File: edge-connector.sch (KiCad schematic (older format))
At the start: 3 parts, among them J5 SFF-TA-1002-4C+

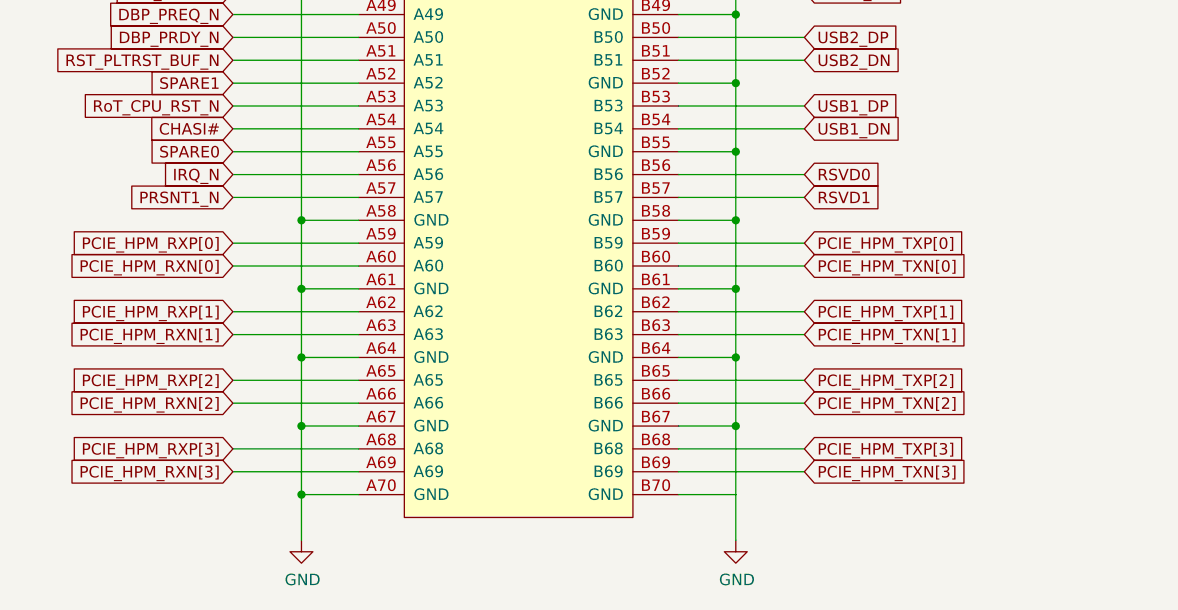
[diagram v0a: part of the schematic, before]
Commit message: Update naming convention for PCIe
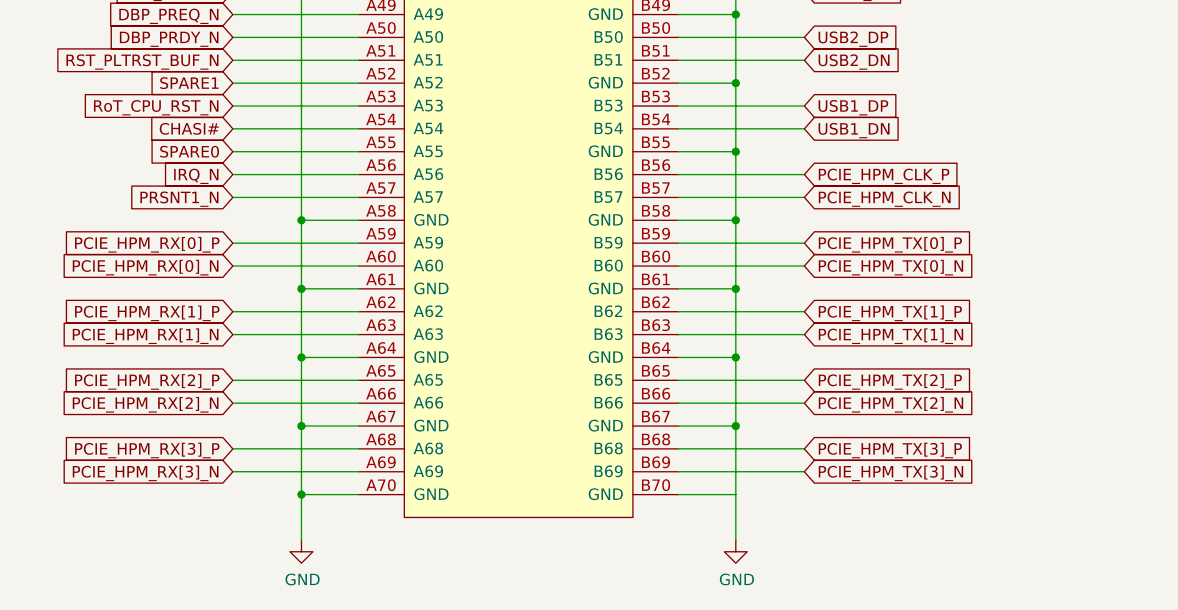
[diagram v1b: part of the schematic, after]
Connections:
- net PCIE_HPM_RXN[0] renamed PCIE_HPM_RX[0]_N
- net PCIE_HPM_RXN[1] renamed PCIE_HPM_RX[1]_N
- net PCIE_HPM_RXN[2] renamed PCIE_HPM_RX[2]_N
- net PCIE_HPM_RXN[3] renamed PCIE_HPM_RX[3]_N
- net PCIE_HPM_RXP[0] renamed PCIE_HPM_RX[0]_P
- net PCIE_HPM_RXP[1] renamed PCIE_HPM_RX[1]_P
- net PCIE_HPM_RXP[2] renamed PCIE_HPM_RX[2]_P
- net PCIE_HPM_RXP[3] renamed PCIE_HPM_RX[3]_P
- net PCIE_HPM_TXN[0] renamed PCIE_HPM_TX[0]_N
- net PCIE_HPM_TXN[1] renamed PCIE_HPM_TX[1]_N
- net PCIE_HPM_TXN[2] renamed PCIE_HPM_TX[2]_N
- net PCIE_HPM_TXN[3] renamed PCIE_HPM_TX[3]_N
- net PCIE_HPM_TXP[0] renamed PCIE_HPM_TX[0]_P
- net PCIE_HPM_TXP[1] renamed PCIE_HPM_TX[1]_P
- net PCIE_HPM_TXP[2] renamed PCIE_HPM_TX[2]_P
- net PCIE_HPM_TXP[3] renamed PCIE_HPM_TX[3]_P
- net RSVD0 renamed PCIE_HPM_CLK_P
- net RSVD1 renamed PCIE_HPM_CLK_N
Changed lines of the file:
@@
 Text GLabel 6625 9125 0    50   Input ~ 0
 PRSNT1_N
-Text GLabel 6625 9325 0    50   Input ~ 0
-PCIE_HPM_RXP[0]
-Text GLabel 6625 9425 0    50   Input ~ 0
-PCIE_HPM_RXN[0]
 Connection ~ 6925 9525
 Wire Wire Line
 	6925 9525 6925 9825
-Text GLabel 6625 9625 0    50   Input ~ 0
-PCIE_HPM_RXP[1]
-Text GLabel 6625 9725 0    50   Input ~ 0
-PCIE_HPM_RXN[1]
-Text GLabel 6625 9925 0    50   Input ~ 0
-PCIE_HPM_RXP[2]
-Text GLabel 6625 10025 0    50   Input ~ 0
-PCIE_HPM_RXN[2]
-Text GLabel 6625 10225 0    50   Input ~ 0
-PCIE_HPM_RXP[3]
-Text GLabel 6625 10325 0    50   Input ~ 0
-PCIE_HPM_RXN[3]
 Text GLabel 9125 1625 2    50   Input ~ 0
 P12V_AUX
@@
 Text GLabel 9125 8825 2    50   Input ~ 0
 USB1_DN
-Text GLabel 9125 9325 2    50   Input ~ 0
-PCIE_HPM_TXP[0]
-Text GLabel 9125 9425 2    50   Input ~ 0
-PCIE_HPM_TXN[0]
-Text GLabel 9125 9625 2    50   Input ~ 0
-PCIE_HPM_TXP[1]
-Text GLabel 9125 9725 2    50   Input ~ 0
-PCIE_HPM_TXN[1]
-Text GLabel 9125 9925 2    50   Input ~ 0
-PCIE_HPM_TXP[2]
-Text GLabel 9125 10025 2    50   Input ~ 0
-PCIE_HPM_TXN[2]
-Text GLabel 9125 10225 2    50   Input ~ 0
-PCIE_HPM_TXP[3]
-Text GLabel 9125 10325 2    50   Input ~ 0
-PCIE_HPM_TXN[3]
-Text GLabel 9125 9025 2    50   Input ~ 0
-RSVD0
-Text GLabel 9125 9125 2    50   Input ~ 0
-RSVD1
 Wire Wire Line
 	8825 10425 8825 10625
@@
 	1    0    0    -1
 $EndComp
+Text GLabel 6625 9325 0    50   Input ~ 0
+PCIE_HPM_RX[0]_P
+Text GLabel 6625 9425 0    50   Input ~ 0
+PCIE_HPM_RX[0]_N
+Text GLabel 6625 9625 0    50   Input ~ 0
+PCIE_HPM_RX[1]_P
+Text GLabel 6625 9725 0    50   Input ~ 0
+PCIE_HPM_RX[1]_N
+Text GLabel 6625 10225 0    50   Input ~ 0
+PCIE_HPM_RX[3]_P
+Text GLabel 6625 10325 0    50   Input ~ 0
+PCIE_HPM_RX[3]_N
+Text GLabel 9125 9625 2    50   Input ~ 0
+PCIE_HPM_TX[1]_P
+Text GLabel 9125 9725 2    50   Input ~ 0
+PCIE_HPM_TX[1]_N
+Text GLabel 9125 9925 2    50   Input ~ 0
+PCIE_HPM_TX[2]_P
+Text GLabel 9125 10025 2    50   Input ~ 0
+PCIE_HPM_TX[2]_N
+Text GLabel 9125 10225 2    50   Input ~ 0
+PCIE_HPM_TX[3]_P
+Text GLabel 9125 10325 2    50   Input ~ 0
+PCIE_HPM_TX[3]_N
+Text GLabel 6625 10025 0    50   Input ~ 0
+PCIE_HPM_RX[2]_N
+Text GLabel 6625 9925 0    50   Input ~ 0
+PCIE_HPM_RX[2]_P
+Text GLabel 9125 9025 2    50   Input ~ 0
+PCIE_HPM_CLK_P
+Text GLabel 9125 9125 2    50   Input ~ 0
+PCIE_HPM_CLK_N
+Text GLabel 9125 9425 2    50   Input ~ 0
+PCIE_HPM_TX[0]_N
+Text GLabel 9125 9325 2    50   Input ~ 0
+PCIE_HPM_TX[0]_P
 $EndSCHEMATC

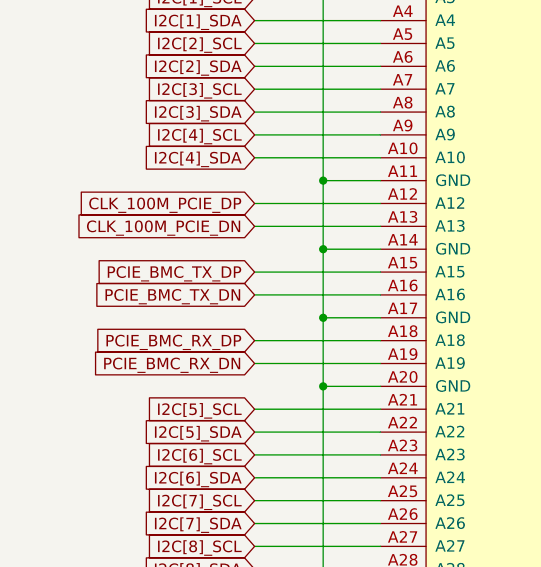
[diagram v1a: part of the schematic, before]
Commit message: Add BMC PCIe net classes
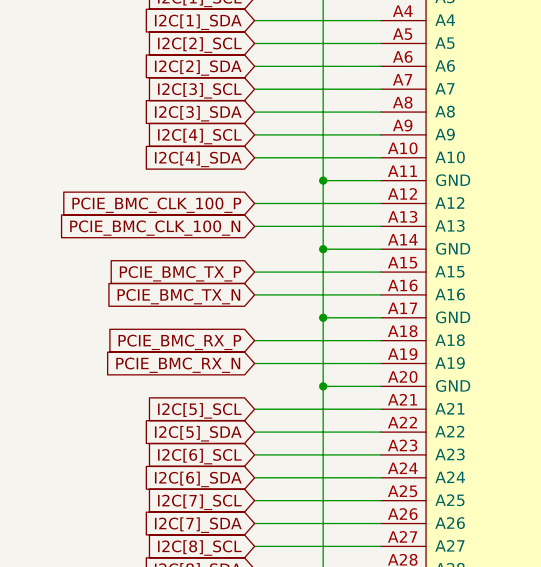
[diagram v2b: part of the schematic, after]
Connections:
- net CLK_100M_PCIE_DN renamed PCIE_BMC_CLK_100_N
- net CLK_100M_PCIE_DP renamed PCIE_BMC_CLK_100_P
- net PCIE_BMC_RX_DN renamed PCIE_BMC_RX_N
- net PCIE_BMC_RX_DP renamed PCIE_BMC_RX_P
- net PCIE_BMC_TX_DN renamed PCIE_BMC_TX_N
- net PCIE_BMC_TX_DP renamed PCIE_BMC_TX_P
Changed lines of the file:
@@
 I2C[4]_SDA
 Text GLabel 6625 4225 0    50   Input ~ 0
-CLK_100M_PCIE_DP
+PCIE_BMC_CLK_100_P
 Text GLabel 6625 4325 0    50   Input ~ 0
-CLK_100M_PCIE_DN
+PCIE_BMC_CLK_100_N
 Text GLabel 6625 4525 0    50   Input ~ 0
-PCIE_BMC_TX_DP
+PCIE_BMC_TX_P
 Text GLabel 6625 4625 0    50   Input ~ 0
-PCIE_BMC_TX_DN
+PCIE_BMC_TX_N
 Text GLabel 6625 4825 0    50   Input ~ 0
-PCIE_BMC_RX_DP
+PCIE_BMC_RX_P
 Text GLabel 6625 4925 0    50   Input ~ 0
-PCIE_BMC_RX_DN
+PCIE_BMC_RX_N
 Text GLabel 6625 5125 0    50   Input ~ 0
 I2C[5]_SCL

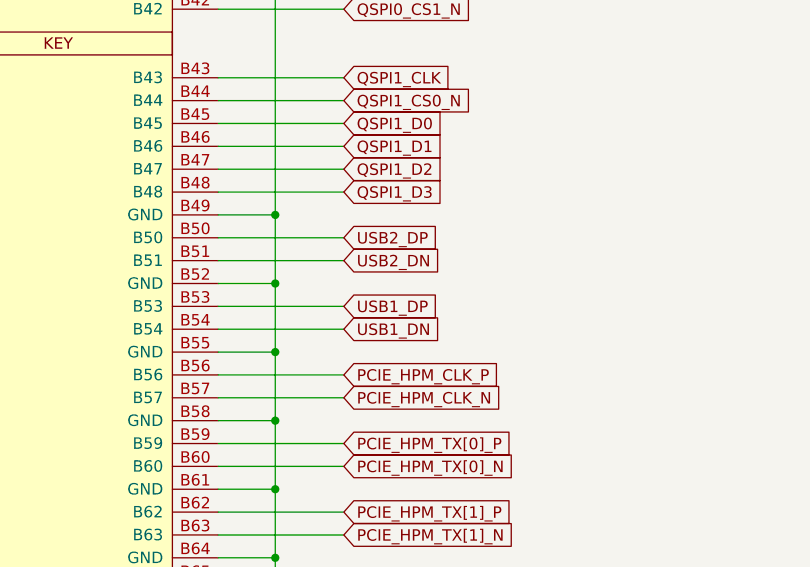
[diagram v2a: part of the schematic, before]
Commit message: Define USB diff lanes
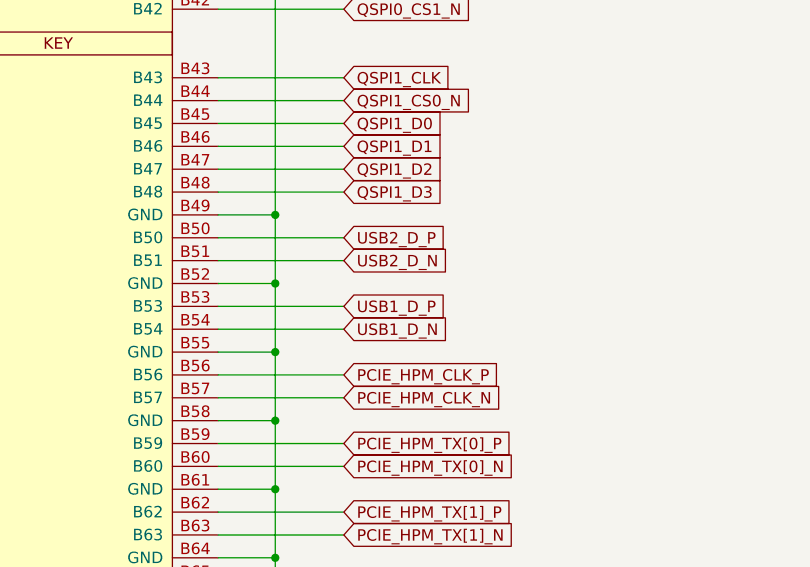
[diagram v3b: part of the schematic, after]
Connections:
- net USB1_DN renamed USB1_D_N
- net USB1_DP renamed USB1_D_P
- net USB2_DN renamed USB2_D_N
- net USB2_DP renamed USB2_D_P
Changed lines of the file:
@@
 QSPI1_D3
 Text GLabel 9125 8425 2    50   Input ~ 0
-USB2_DP
+USB2_D_P
 Text GLabel 9125 8525 2    50   Input ~ 0
-USB2_DN
+USB2_D_N
 Connection ~ 8825 8625
 Wire Wire Line
 	8825 8625 8825 8925
 Text GLabel 9125 8725 2    50   Input ~ 0
-USB1_DP
+USB1_D_P
 Text GLabel 9125 8825 2    50   Input ~ 0
-USB1_DN
+USB1_D_N
 Wire Wire Line
 	8825 10425 8825 10625

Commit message: Typo fix
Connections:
- net SPIO_CLK renamed SPI0_CLK
- net SPIO_CS_N renamed SPI0_CS_N
- net SPIO_MISO renamed SPI0_MISO
- net SPIO_MOSI renamed SPI0_MOSI
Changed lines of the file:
@@
 UART0_SCM_RX
 Text GLabel 9125 2525 2    50   Input ~ 0
-SPIO_CLK
+SPI0_CLK
 Text GLabel 9125 2625 2    50   Input ~ 0
-SPIO_CS_N
+SPI0_CS_N
 Text GLabel 9125 2725 2    50   Input ~ 0
-SPIO_MOSI
+SPI0_MOSI
 Text GLabel 9125 2825 2    50   Input ~ 0
-SPIO_MISO
+SPI0_MISO
 Text GLabel 9125 3125 2    50   Input ~ 0
 ESPI_CLK

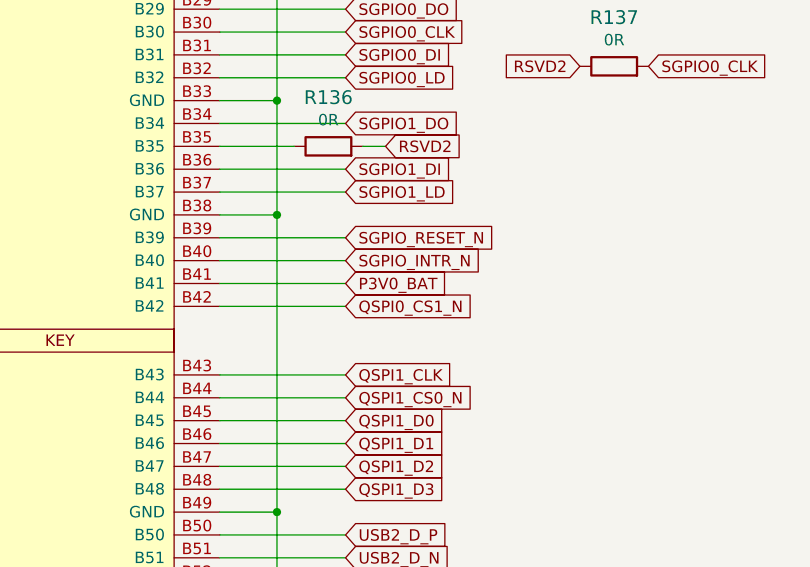
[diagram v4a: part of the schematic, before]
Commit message: Update schematic notes, update SPI0 connection
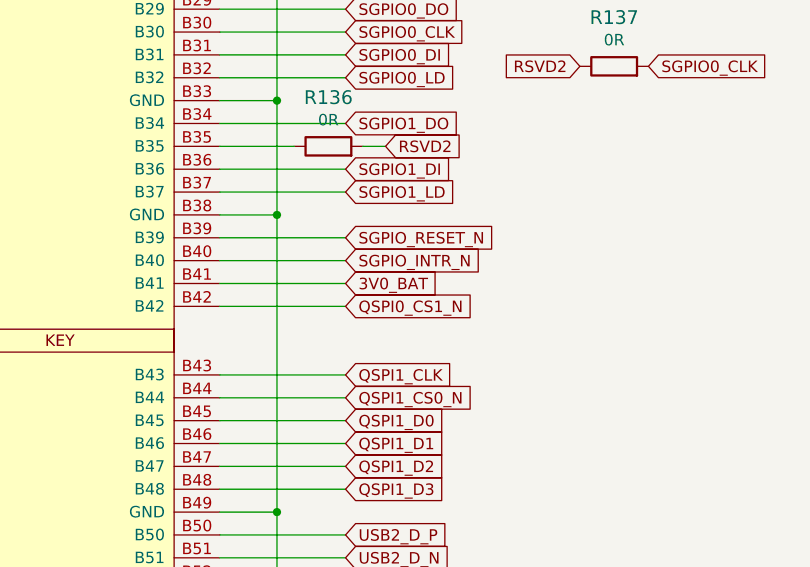
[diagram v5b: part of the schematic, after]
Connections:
- net P3V0_BAT renamed 3V0_BAT
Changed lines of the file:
@@
 SGPIO_INTR_N
 Text GLabel 9125 7325 2    50   Input ~ 0
-P3V0_BAT
+3V0_BAT
 Text GLabel 9125 7425 2    50   Input ~ 0
 QSPI0_CS1_N

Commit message: Cleaned up schematics
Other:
- moved on the sheet: R137
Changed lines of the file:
@@
 Wire Wire Line
 	8825 10425 8575 10425
-Text Notes 7175 925  0    118  ~ 0
+Text Notes 7175 925  0    118  ~ 24
 Edge connector
 Text GLabel 9125 1925 2    50   Input ~ 0
@@
 Wire Wire Line
 	8575 6225 9125 6225
-Text GLabel 10150 6375 0    50   Input ~ 0
+Text GLabel 10125 6725 0    50   Input ~ 0
 RSVD2
-Text GLabel 10450 6375 2    50   Input ~ 0
+Text GLabel 10425 6725 2    50   Input ~ 0
 SGPIO0_CLK
 $Comp
 L artix-dc-scm:R_0R_0402 R137
 U 1 1 617019A6
-P 10300 6375
-F 0 "R137" H 10300 6588 60  0000 C CNN
-F 1 "R_0R_0402" H 10300 6225 60  0001 C CNN
-F 2 "artix-dc-scm-footprints:0402-res" H 10500 6575 60  0001 L CNN
-F 3 "" H 10300 6375 50  0001 C CNN
-F 4 "PANASONIC" H 10500 6775 60  0001 L CNN "Manufacturer"
-F 5 "ERJ2GE0R00X" H 10500 6675 60  0001 L CNN "MPN"
-F 6 "0R" H 10300 6490 50  0000 C CNN "Val"
-	1    10300 6375
+P 10275 6725
+F 0 "R137" H 10275 6938 60  0000 C CNN
+F 1 "R_0R_0402" H 10275 6575 60  0001 C CNN
+F 2 "artix-dc-scm-footprints:0402-res" H 10475 6925 60  0001 L CNN
+F 3 "" H 10275 6725 50  0001 C CNN
+F 4 "PANASONIC" H 10475 7125 60  0001 L CNN "Manufacturer"
+F 5 "ERJ2GE0R00X" H 10475 7025 60  0001 L CNN "MPN"
+F 6 "0R" H 10275 6840 50  0000 C CNN "Val"
+	1    10275 6725
 	1    0    0    -1
 $EndComp
